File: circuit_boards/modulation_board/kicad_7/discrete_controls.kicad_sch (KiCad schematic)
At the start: 26 parts, among them SW11 E-Switch_EG2301B, SW508 5511M12, U6 74HC4067PW, U803 MCP6002-xSN

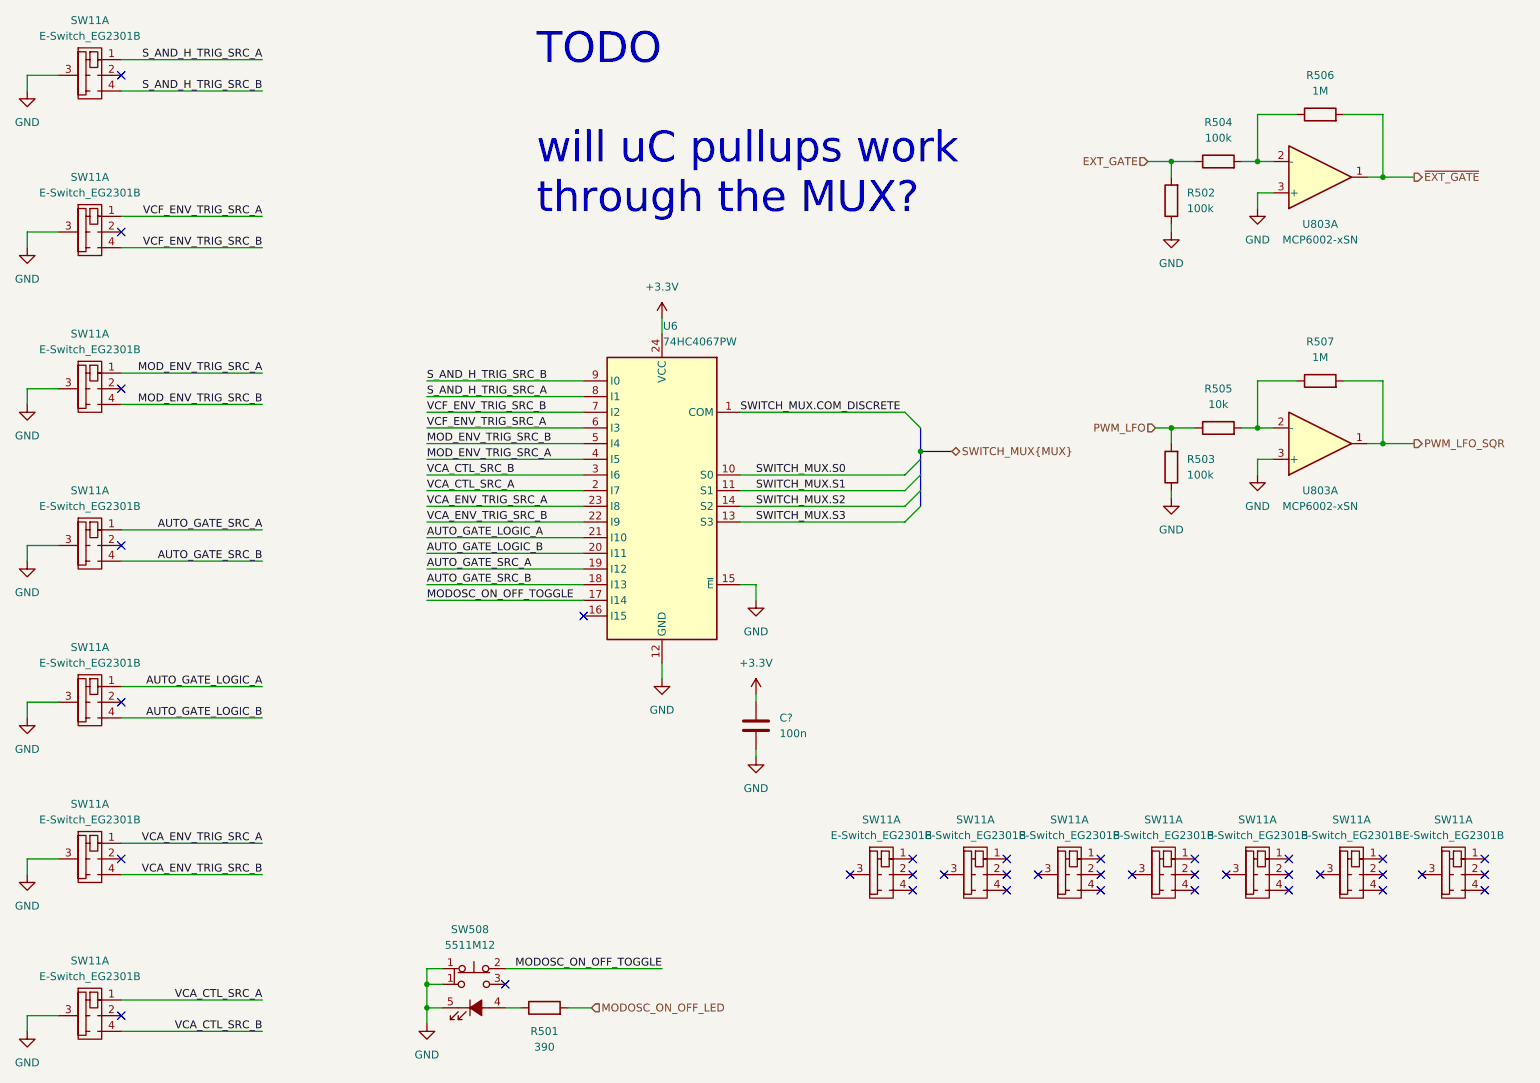
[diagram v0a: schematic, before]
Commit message: Tweaks to mod board, debounce MODOSC toggle switch
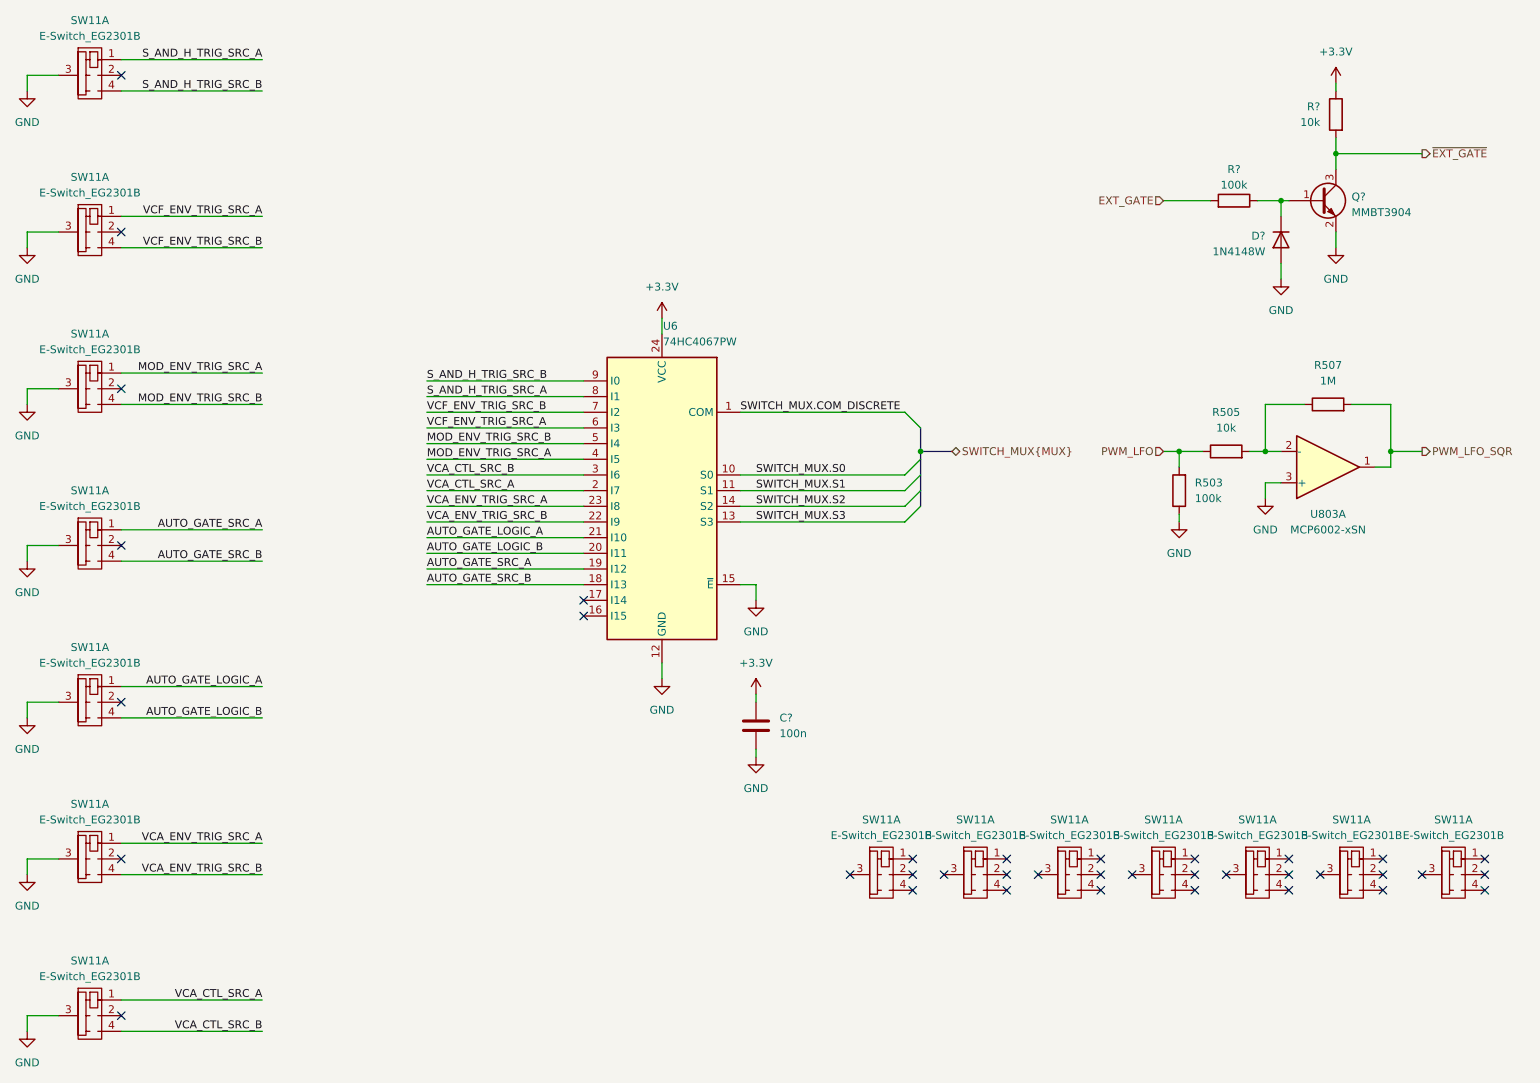
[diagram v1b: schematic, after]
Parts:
- removed R501: 390, Resistor_SMD:R_0603_1608Metric, symbol Device:R
- removed R502, R504: 100k, Resistor_SMD:R_0603_1608Metric, symbol Device:R
- removed R506: 1M, Resistor_SMD:R_0603_1608Metric, symbol Device:R
- removed SW508: 5511M12, custom_footprints:E_Switch_5511M12, symbol custom_symbols:E_Switch_5511M12
- removed U803: MCP6002-xSN, Package_SO:SOIC-8_3.9x4.9mm_P1.27mm, symbol Amplifier_Operational:MCP6002-xSN
- added D?: 1N4148W, Diode_SMD:D_SOD-123, symbol Diode:1N4148W
- added Q?: MMBT3904, Package_TO_SOT_SMD:SOT-23, symbol Transistor_BJT:MMBT3904
- added R?: 10k, Resistor_SMD:R_0603_1608Metric, symbol Device:R
- added R?: 100k, Resistor_SMD:R_0603_1608Metric, symbol Device:R
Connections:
- net +3.3V: now also R?.1
- net EXT_GATE: now also R?.2
- net GND: now also D?.2 (A), Q?.2 (E)
- net ~{EXT_GATE}: now also Q?.3 (C), R?.2
- net MODOSC_ON_OFF_TOGGLE: no longer names the net of U6.17 (I14)
- new net: D?.1 (K), Q?.1 (B), R?.1
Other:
- note removed: "TODO will uC pullups work through the MUX?"
- moved on the sheet: R503, R505, R507, U803A
